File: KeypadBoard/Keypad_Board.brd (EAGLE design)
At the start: 45.8 x 44.5 mm, 31 parts, among them Q1 4.3A/20V/54mΩ, U1 ESP32-WROOM-32E_(16MB), U2 LTC1730ES8-4.2#TRPBF

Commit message: Board Rev2
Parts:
- added J8: (no value), SparkFun-Connectors:1X05
- moved J1 6.35 mm to (54.6, 55.9)
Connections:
- new net BTN1: J8.3, U1.23
- new net X_AXIS: J8.5, U1.6
- new net Y_AXIS: J8.4, U1.7
- net 3V3: now also J8.1
- net GND: now also J8.2
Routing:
- net Y_AXIS: track 0.00 -> 47.8 mm, vias 0 -> 1
- net X_AXIS: track 0.00 -> 41.8 mm, vias 0 -> 2
- net BTN1: track 0.00 -> 17.5 mm, vias 0 -> 2
- net 3V3: track 65.8 -> 83.2 mm
- net ROW1: track 13.2 -> 7.12 mm
- net ROW3: track 12.2 -> 6.60 mm
- net ROW2: track 12.1 -> 6.60 mm
- net ROW4: track 10.9 -> 6.07 mm
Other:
- board text added: "BOOT"
- board text added: "RST"

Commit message: Board updates - ADC OverVoltage fix
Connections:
- net BAT: no longer U1.8
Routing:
- net BAT: track 26.6 -> 14.5 mm
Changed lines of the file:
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@@
 </signal>
 <signal name="BAT">
-<contactref element="U1" pad="8"/>
 <contactref element="U2" pad="8"/>
 <contactref element="Q1" pad="3"/>
 <contactref element="J6" pad="2"/>
-<wire x1="22.86" y1="61.13" x2="28.872" y2="61.13" width="0.508" layer="1"/>
-<wire x1="28.872" y1="61.13" x2="29.972" y2="62.23" width="0.508" layer="1"/>
-<wire x1="29.972" y1="62.23" x2="29.972" y2="64.262" width="0.508" layer="1"/>
-<wire x1="30.66" y1="64.95" x2="32.14" y2="64.95" width="0.508" layer="1"/>
-<wire x1="29.972" y1="64.262" x2="30.66" y2="64.95" width="0.508" layer="1"/>
 <wire x1="22.86" y1="61.13" x2="22.69" y2="60.96" width="0.508" layer="1"/>
 <wire x1="22.69" y1="60.96" x2="17.78" y2="60.96" width="0.508" layer="1"/>

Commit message: Added battery level monitoring and charge LED
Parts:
- added R12: 330K, SparkFun-Resistors:0805
- added R13: 120K, SparkFun-Resistors:0805
- R4, R7: value 1K -> 330
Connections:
- new net BAT_ADC: R12.1, R13.2, U1.8
- net 3V3: now also J3.4
- net BAT: now also R13.1
- net GND: now also R12.2; no longer J3.4
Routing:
- net BAT_ADC: track 0.00 -> 15.3 mm
- net 3V3: track 83.2 -> 91.8 mm
- net BAT: track 14.5 -> 20.3 mm
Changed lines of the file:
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@@
 <attribute name="VALUE" x="26.797" y="64.77" size="0.6096" layer="27" font="vector" ratio="20" rot="R270" align="top-center"/>
 </element>
-<element name="R4" library="SparkFun-Resistors" library_urn="urn:adsk.eagle:library:532" package="0805" package3d_urn="urn:adsk.eagle:package:39651/1" value="1K" x="17.78" y="50.8" smashed="yes">
+<element name="R4" library="SparkFun-Resistors" library_urn="urn:adsk.eagle:library:532" package="0805" package3d_urn="urn:adsk.eagle:package:39651/1" value="330" x="17.78" y="50.8" smashed="yes">
 <attribute name="NAME" x="16.51" y="49.911" size="0.6096" layer="25" font="vector" ratio="20" rot="R180" align="bottom-center"/>
 <attribute name="PROD_ID" value="RES-09883" x="57.15" y="-5.08" size="1.778" layer="27" display="off"/>
@@
 <attribute name="VALUE" x="17.018" y="64.77" size="0.6096" layer="27" font="vector" ratio="20" rot="R270" align="top-center"/>
 </element>
-<element name="R7" library="SparkFun-Resistors" library_urn="urn:adsk.eagle:library:532" package="0805" package3d_urn="urn:adsk.eagle:package:39651/1" value="1K" x="17.78" y="45.72" smashed="yes">
+<element name="R7" library="SparkFun-Resistors" library_urn="urn:adsk.eagle:library:532" package="0805" package3d_urn="urn:adsk.eagle:package:39651/1" value="330" x="17.78" y="45.72" smashed="yes">
 <attribute name="NAME" x="17.78" y="46.609" size="0.6096" layer="25" font="vector" ratio="20" align="bottom-center"/>
 <attribute name="PROD_ID" value="RES-09883" x="64.77" y="-10.16" size="1.778" layer="27" display="off"/>
@@
 <attribute name="NAME" x="53.213" y="41.91" size="0.6096" layer="25" font="vector" ratio="20" rot="R90"/>
 <attribute name="VALUE" x="56.642" y="41.91" size="0.6096" layer="27" font="vector" ratio="20" rot="R90"/>
+</element>
+<element name="R12" library="SparkFun-Resistors" library_urn="urn:adsk.eagle:library:532" package="0805" package3d_urn="urn:adsk.eagle:package:39651/1" value="330K" x="29.21" y="52.07" smashed="yes" rot="R180">
+<attribute name="NAME" x="29.21" y="51.181" size="0.6096" layer="25" font="vector" ratio="20" rot="R180" align="bottom-center"/>
+<attribute name="PROD_ID" value="RES-09883" x="29.21" y="52.07" size="1.778" layer="27" rot="R180" display="off"/>
+<attribute name="VALUE" x="29.21" y="52.959" size="0.6096" layer="27" font="vector" ratio="20" rot="R180" align="top-center"/>
+</element>
+<element name="R13" library="SparkFun-Resistors" library_urn="urn:adsk.eagle:library:532" package="0805" package3d_urn="urn:adsk.eagle:package:39651/1" value="120K" x="28.575" y="60.198" smashed="yes" rot="R270">
+<attribute name="NAME" x="29.464" y="60.198" size="0.6096" layer="25" font="vector" ratio="20" rot="R270" align="bottom-center"/>
+<attribute name="PROD_ID" value="RES-09883" x="28.575" y="60.198" size="1.778" layer="27" rot="R270" display="off"/>
+<attribute name="VALUE" x="27.686" y="60.198" size="0.6096" layer="27" font="vector" ratio="20" rot="R270" align="top-center"/>
 </element>
 </elements>
@@
 <contactref element="J5" pad="2"/>
 <contactref element="J3" pad="2"/>
-<contactref element="J3" pad="4"/>
 <contactref element="S1" pad="1"/>
 <contactref element="S2" pad="1"/>
@@
 </polygon>
 <contactref element="J8" pad="2"/>
+<contactref element="R12" pad="2"/>
 </signal>
 <signal name="BAT">
@@
 <via x="17.78" y="59.69" extent="1-16" drill="0.35"/>
 <wire x1="17.78" y1="59.69" x2="17.78" y2="60.96" width="0.508" layer="1"/>
+<contactref element="R13" pad="1"/>
+<wire x1="28.575" y1="61.098" x2="22.892" y2="61.098" width="0.1524" layer="1"/>
+<wire x1="22.892" y1="61.098" x2="22.86" y2="61.13" width="0.1524" layer="1"/>
 </signal>
 <signal name="VCC">
@@
 <wire x1="41.91" y1="43.18" x2="40.64" y2="44.45" width="0.1524" layer="1"/>
 <wire x1="40.64" y1="44.45" x2="40.64" y2="47.36" width="0.1524" layer="1"/>
+<contactref element="J3" pad="4"/>
+<wire x1="13.97" y1="43.18" x2="16.51" y2="43.18" width="0.1524" layer="16"/>
+<wire x1="19.05" y1="45.72" x2="19.05" y2="48.26" width="0.1524" layer="16"/>
+<wire x1="16.51" y1="43.18" x2="19.05" y2="45.72" width="0.1524" layer="16"/>
 </signal>
 <signal name="N$9">
@@
 <wire x1="45.085" y1="57.785" x2="45.085" y2="56.33" width="0.1524" layer="1"/>
 </signal>
+<signal name="BAT_ADC">
+<contactref element="R12" pad="1"/>
+<contactref element="R13" pad="2"/>
+<contactref element="U1" pad="8"/>
+<wire x1="28.575" y1="59.298" x2="30.48" y2="61.203" width="0.1524" layer="1"/>
+<wire x1="30.48" y1="63.7932875" x2="31.6367125" y2="64.95" width="0.1524" layer="1"/>
+<wire x1="31.6367125" y1="64.95" x2="32.14" y2="64.95" width="0.1524" layer="1"/>
+<wire x1="30.48" y1="61.203" x2="30.48" y2="63.7932875" width="0.1524" layer="1"/>
+<wire x1="28.575" y1="59.298" x2="30.11" y2="57.763" width="0.1524" layer="1"/>
+<wire x1="30.11" y1="57.763" x2="30.11" y2="52.07" width="0.1524" layer="1"/>
+</signal>
 </signals>

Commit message: Updated board for connection of a Micro SD Card module
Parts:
- added J9: (no value), SparkFun-Connectors:1X06_LOCK
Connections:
- new net CLK: U1.13
- new net CS: J9.1, U1.23
- new net MISO: J9.4, U1.14
- new net MOSI: J9.3, U1.16
- new net SCK: J9.2
- net 3V3: no longer J3.4
- net BTN1: now also U1.29; no longer U1.23
- net GND: now also J9.6
- net VCC: now also J9.5
- net VUSB: now also J3.4
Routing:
- net VUSB: track 67.3 -> 80.6 mm, vias 3 -> 4
- net 3V3: track 91.8 -> 83.2 mm
- net BTN1: track 17.5 -> 16.0 mm
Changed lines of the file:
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@@
 <attribute name="VALUE" x="27.686" y="60.198" size="0.6096" layer="27" font="vector" ratio="20" rot="R270" align="top-center"/>
+</element>
+<element name="J9" library="SparkFun-Connectors" library_urn="urn:adsk.eagle:library:513" package="1X06_LOCK" package3d_urn="urn:adsk.eagle:package:38002/1" value="" x="13.97" y="38.1" smashed="yes">
+<attribute name="NAME" x="12.7" y="39.497" size="0.6096" layer="25" font="vector" ratio="20"/>
+<attribute name="VALUE" x="12.7" y="35.814" size="0.6096" layer="27" font="vector" ratio="20"/>
 </element>
 </elements>
@@
 <contactref element="J8" pad="2"/>
 <contactref element="R12" pad="2"/>
+<contactref element="J9" pad="6"/>
+<wire x1="26.67" y1="46.86" x2="26.67" y2="37.846" width="0" layer="19" extent="1-1"/>
 </signal>
 <signal name="BAT">
@@
 <wire x1="12.446" y1="78.232" x2="15.108" y2="75.57" width="0.1524" layer="1"/>
 <wire x1="15.108" y1="75.57" x2="16.15" y2="75.57" width="0.1524" layer="1"/>
+<contactref element="J9" pad="5"/>
+<wire x1="24.13" y1="38.1" x2="21.91" y2="63.23" width="0" layer="19" extent="1-1"/>
 </signal>
 <signal name="ADJ">
@@
 <wire x1="21.082" y1="53.975" x2="22.225" y2="52.832" width="0.1524" layer="1"/>
 <wire x1="22.225" y1="52.832" x2="22.225" y2="52.1462" width="0.1524" layer="1"/>
+<contactref element="J3" pad="4"/>
+<wire x1="13.97" y1="43.18" x2="20.32" y2="43.18" width="0.1524" layer="16"/>
+<wire x1="20.32" y1="43.18" x2="22.86" y2="45.72" width="0.1524" layer="16"/>
+<wire x1="22.86" y1="45.72" x2="22.86" y2="46.863" width="0.1524" layer="16"/>
+<wire x1="22.86" y1="46.863" x2="22.225" y2="47.498" width="0.1524" layer="16"/>
+<via x="22.225" y="47.498" extent="1-16" drill="0.35"/>
+<wire x1="22.225" y1="47.498" x2="21.043" y2="47.498" width="0.1524" layer="1"/>
+<wire x1="21.043" y1="47.498" x2="20.955" y2="47.41" width="0.1524" layer="1"/>
 </signal>
 <signal name="3V3">
@@
 <wire x1="41.91" y1="43.18" x2="40.64" y2="44.45" width="0.1524" layer="1"/>
 <wire x1="40.64" y1="44.45" x2="40.64" y2="47.36" width="0.1524" layer="1"/>
-<contactref element="J3" pad="4"/>
-<wire x1="13.97" y1="43.18" x2="16.51" y2="43.18" width="0.1524" layer="16"/>
-<wire x1="19.05" y1="45.72" x2="19.05" y2="48.26" width="0.1524" layer="16"/>
-<wire x1="16.51" y1="43.18" x2="19.05" y2="45.72" width="0.1524" layer="16"/>
 </signal>
 <signal name="N$9">
@@
 <signal name="BTN1">
 <contactref element="J8" pad="3"/>
-<contactref element="U1" pad="23"/>
 <wire x1="54.61" y1="48.26" x2="53.34" y2="48.26" width="0.1524" layer="1"/>
 <wire x1="53.34" y1="48.26" x2="50.8" y2="50.8" width="0.1524" layer="1"/>
@@
 <via x="44.45" y="58.42" extent="1-16" drill="0.35"/>
 <wire x1="44.45" y1="58.42" x2="45.085" y2="57.785" width="0.1524" layer="1"/>
-<wire x1="45.085" y1="57.785" x2="45.085" y2="56.33" width="0.1524" layer="1"/>
+<contactref element="U1" pad="29"/>
+<wire x1="44.45" y1="58.42" x2="49.14" y2="62.41" width="0" layer="19" extent="1-1"/>
 </signal>
 <signal name="BAT_ADC">
@@
 <wire x1="30.11" y1="57.763" x2="30.11" y2="52.07" width="0.1524" layer="1"/>
 </signal>
+<signal name="MISO">
+<contactref element="U1" pad="14"/>
+<contactref element="J9" pad="4"/>
+<wire x1="21.59" y1="37.846" x2="32.14" y2="57.33" width="0" layer="19" extent="1-1"/>
+</signal>
+<signal name="MOSI">
+<contactref element="U1" pad="16"/>
+<contactref element="J9" pad="3"/>
+<wire x1="19.05" y1="38.1" x2="36.195" y2="56.33" width="0" layer="19" extent="1-1"/>
+</signal>
+<signal name="CLK">
+<contactref element="U1" pad="13"/>
+</signal>
+<signal name="CS">
+<contactref element="U1" pad="23"/>
+<contactref element="J9" pad="1"/>
+<wire x1="13.97" y1="38.1" x2="45.085" y2="56.33" width="0" layer="19" extent="1-1"/>
+</signal>
+<signal name="SCK">
+<contactref element="J9" pad="2"/>
+</signal>
 </signals>

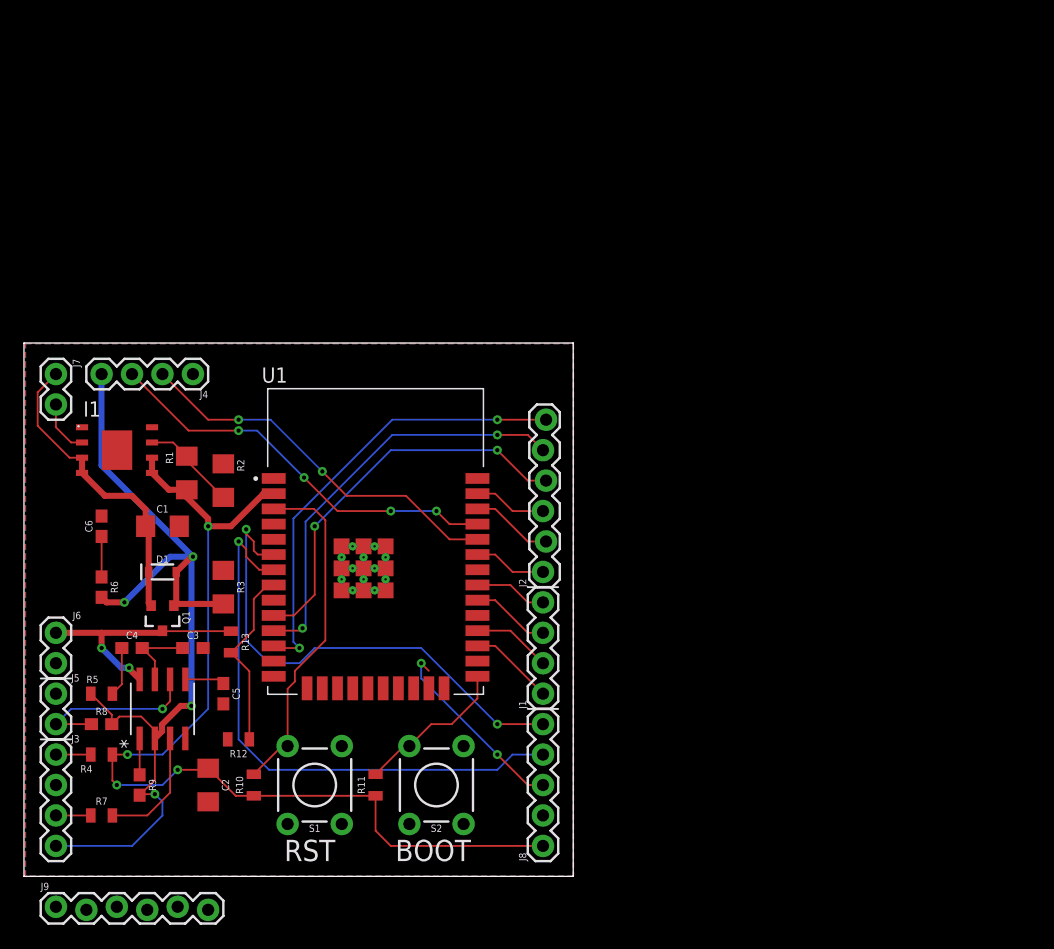
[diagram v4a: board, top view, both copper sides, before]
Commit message: Board V4 - integrated battery holder, SD Breakout, mode LED's
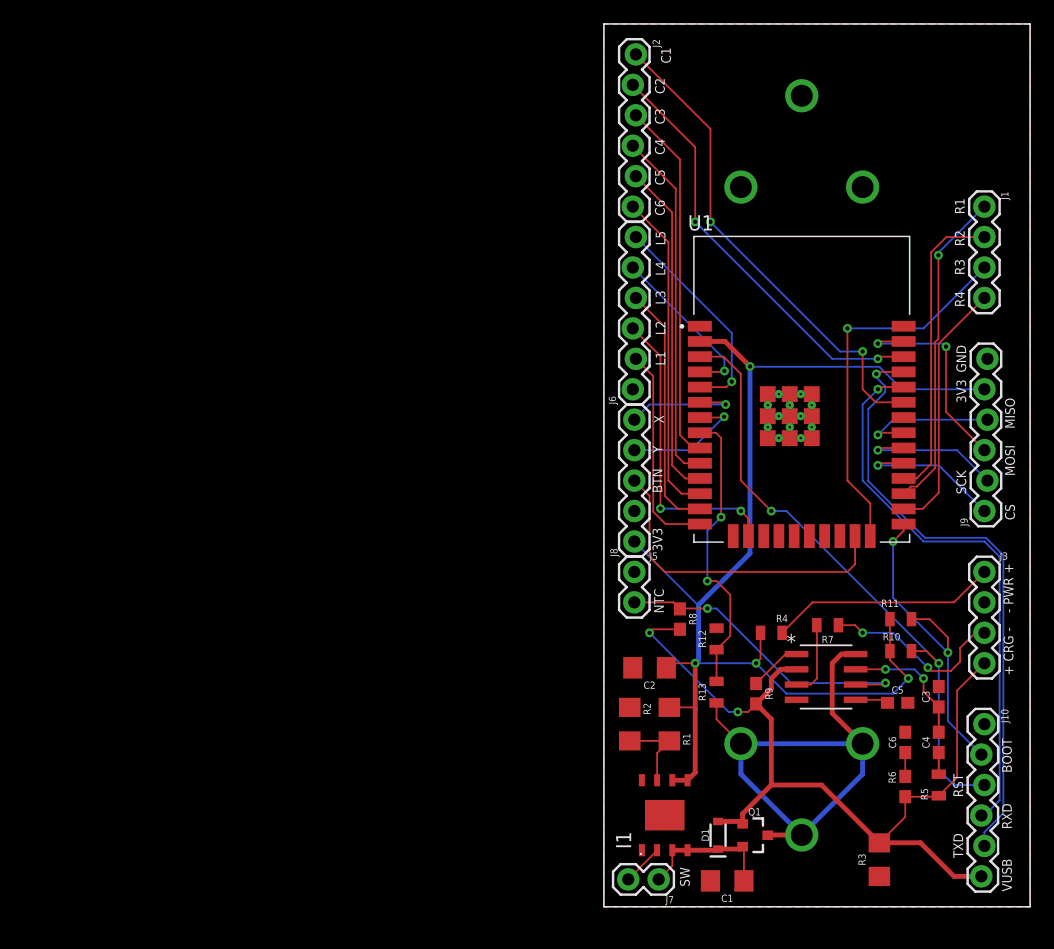
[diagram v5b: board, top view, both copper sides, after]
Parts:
- removed J4: (no value), SparkFun-Connectors:1X04
- removed S1, S2: MOMENTARY-SWITCH-SPST-PTH-6.0MM, SparkFun-Switches:TACTILE_SWITCH_PTH_6.0MM
- added BT1, BT2: KEYSTONE_54KEYSTONE_54_0_0, Keystone - 54:KEYSTONE_54_0
- added J10: (no value), SparkFun-Connectors:1X06_LOCK
- J6: device SparkFun-Connectors:1X02 -> SparkFun-Connectors:1X06_LOCK
- moved J9 84.2 mm to (91.4, 71.1), turned to 90 degrees
- moved J3 79.0 mm to (91.4, 66.0)
- moved R5 70.3 mm to (87.6, 48.3), turned to 90 degrees
- moved C6 69.4 mm to (84.8, 51.8)
- moved R6 69.1 mm to (84.8, 48.1)
- moved C4 67.8 mm to (87.6, 51.8), turned to 90 degrees
- moved J7 65.6 mm to (64.3, 40.4), turned to 180 degrees
- moved R7 62.6 mm to (78.4, 61.6), turned to 180 degrees
- moved C3 62.4 mm to (87.6, 55.6), turned to 90 degrees
- moved R3 59.3 mm to (82.7, 42.0), turned to 90 degrees
- moved R4 56.8 mm to (73.7, 61.0), turned to 180 degrees
- moved C5 56.3 mm to (84.2, 55.1), turned to 0 degrees
- moved C1 55.6 mm to (70.0, 40.3), turned to 180 degrees
- moved U2 55.4 mm to (78.2, 57.3), turned to 0 degrees
- moved R10 55.1 mm to (84.5, 59.4), turned to 0 degrees
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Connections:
- removed net CLK: U1.13
- new net LED1: J6.2, U1.14
- new net LED2: J6.3, U1.16
- new net LED3: J6.4, U1.13
- new net LED4: J6.5, U1.4
- new net LED5: J6.6, U1.5
- net 3V3: now also J9.5
- net BAT: now also BT1.1, BT1.1-2, BT1.1-3; no longer J6.2
- net BOOT: now also J10.2; no longer S2.3
- net BTN1: now also U1.23; no longer U1.29
- net COL3: now also U1.9; no longer U1.37
- net CS: now also U1.29; no longer U1.23
- net GND: now also BT2.1, BT2.1-2, BT2.1-3, J10.1; no longer J4.1, S1.1, S2.1
- net MISO: now also U1.31; no longer U1.14
- net MOSI: now also U1.37; no longer U1.16
- net ROW3: now also U1.24; no longer U1.30
- net ROW4: now also U1.26; no longer U1.31
- net RST: now also J10.3; no longer S1.3
- net RXD: now also J10.4; no longer J4.2
- net SCK: now also U1.30
- net TXD: now also J10.5; no longer J4.3
- net VCC: no longer J9.5
- net VUSB: now also J10.6; no longer J4.4
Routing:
- net Y_AXIS: track 47.8 -> 10.7 mm
- net COL1: track 6.07 -> 40.7 mm, vias 0 -> 2
- net X_AXIS: track 41.8 -> 10.4 mm, vias 2 -> 1
- net COL2: track 6.85 -> 35.8 mm, vias 0 -> 2
- net BAT: track 20.3 -> 46.7 mm, vias 2 -> 0
- net LED2: track 0.00 -> 25.1 mm, vias 0 -> 2
- net ROW3: track 6.60 -> 31.7 mm, vias 0 -> 1
- net COL3: track 6.07 -> 30.3 mm
- net RST: track 28.6 -> 51.7 mm, vias 0 -> 2
- net LED3: track 0.00 -> 20.9 mm
- net 3V3: track 83.2 -> 103.3 mm
- net ROW1: track 7.12 -> 27.0 mm, vias 0 -> 1
- net ROW2: track 6.60 -> 25.4 mm
- net LED5: track 0.00 -> 18.2 mm, vias 0 -> 1
- net MOSI: track 0.00 -> 18.0 mm, vias 0 -> 2
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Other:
- board size 45.8 x 44.5 mm -> 35.6 x 73.7 mm
- board text added: "+ CRG -"
- board text added: "- PWR +"
- board text added: "3V3"
- board text added: "BTN"
- board text added: "C1"
- board text added: "C2"
- board text added: "C3"
- board text added: "C4"
- board text added: "C5"
- board text added: "C6"
- board text added: "CS"
- board text added: "GND"
- board text added: "L1"
- board text added: "L2"
- board text added: "L3"
- board text added: "L4"
- board text added: "L5"
- board text added: "MISO"
- board text added: "MOSI"
- board text added: "NTC"
- board text added: "R1"
- board text added: "R2"
- board text added: "R3"
- board text added: "R4"
- board text added: "RXD"
- board text added: "SCK"
- board text added: "SW"
- board text added: "TXD"
- board text added: "VUSB"
- board text added: "X"
- board text added: "Y"
